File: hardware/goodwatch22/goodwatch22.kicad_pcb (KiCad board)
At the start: 2 copper layers, 25.6 x 27.6 mm, 20 parts, among them U1 CC430F613x, Y1 32.768kHz, Y2 FA128

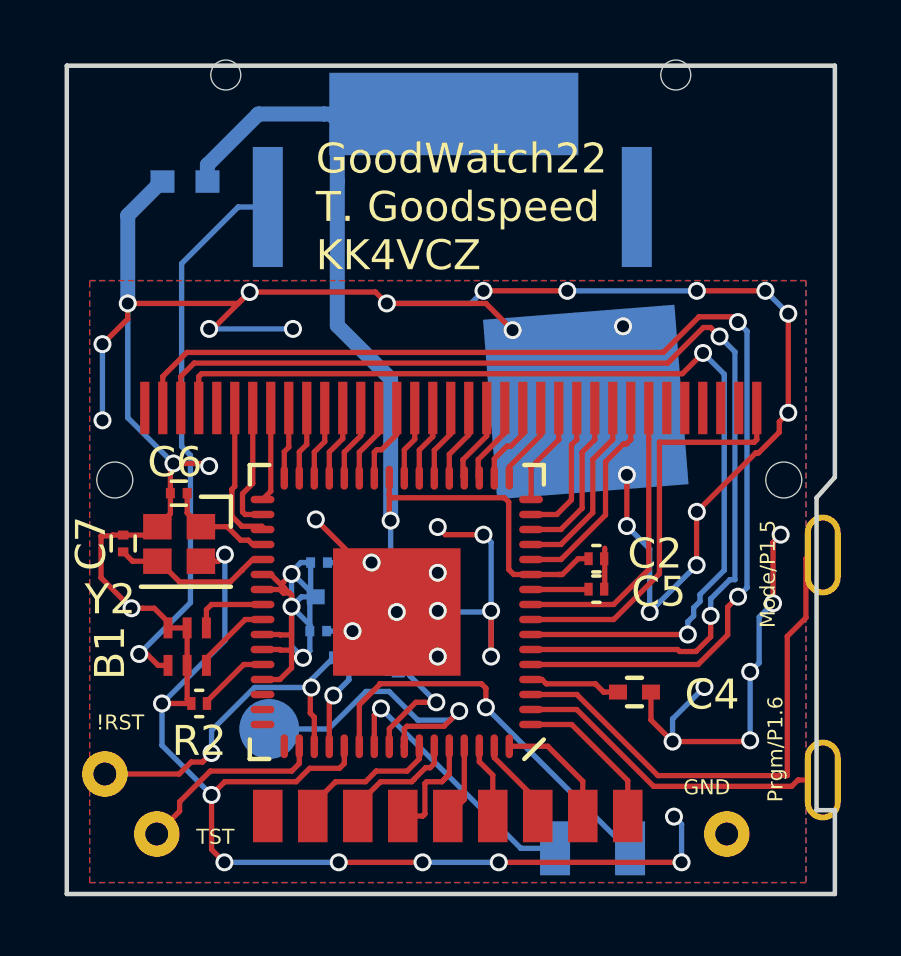
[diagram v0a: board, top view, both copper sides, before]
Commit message: Minor repositioning of silkscreen text and ground connections. #95
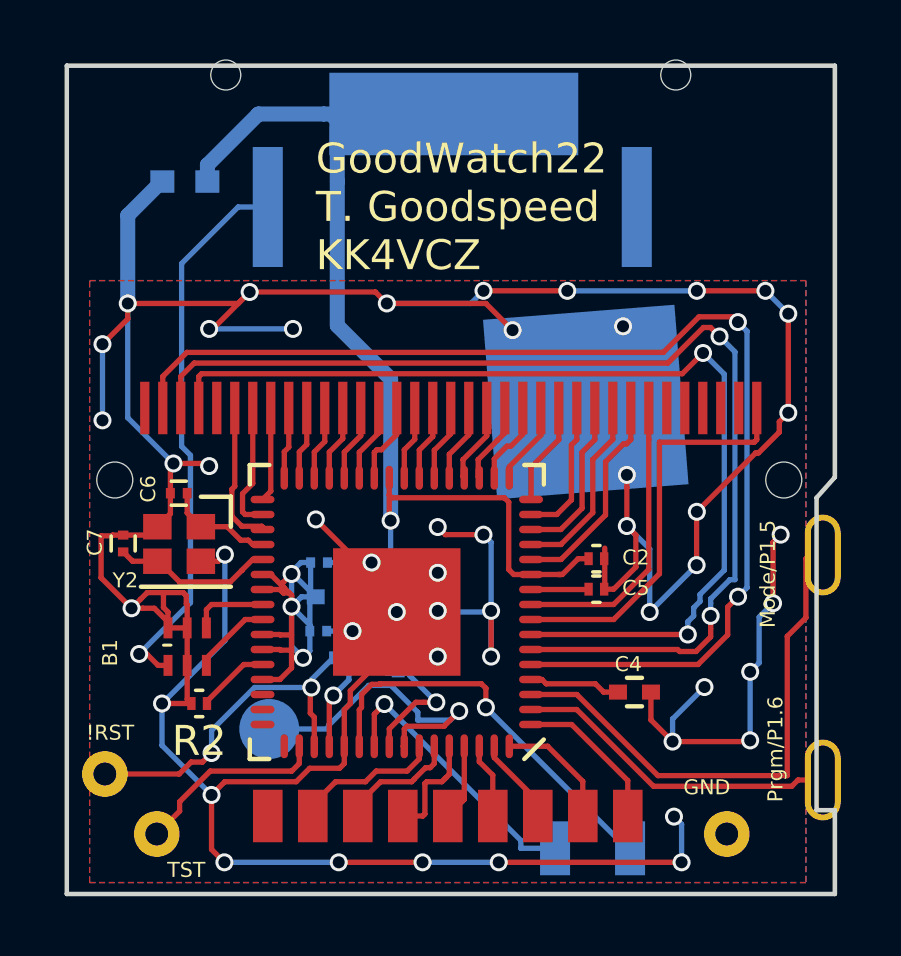
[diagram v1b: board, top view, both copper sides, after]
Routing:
- net GND: track 155.7 -> 168.2 mm
